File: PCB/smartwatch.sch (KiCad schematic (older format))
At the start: 66 parts, among them U1 STM32F103C8T6, U2 HM-10_MIN, U3 M25P40, U4 BMC150, U5 BMP180, U6 STC4054, U7 NCP551, U8 SH1106, X1 VIN, X10 3V3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

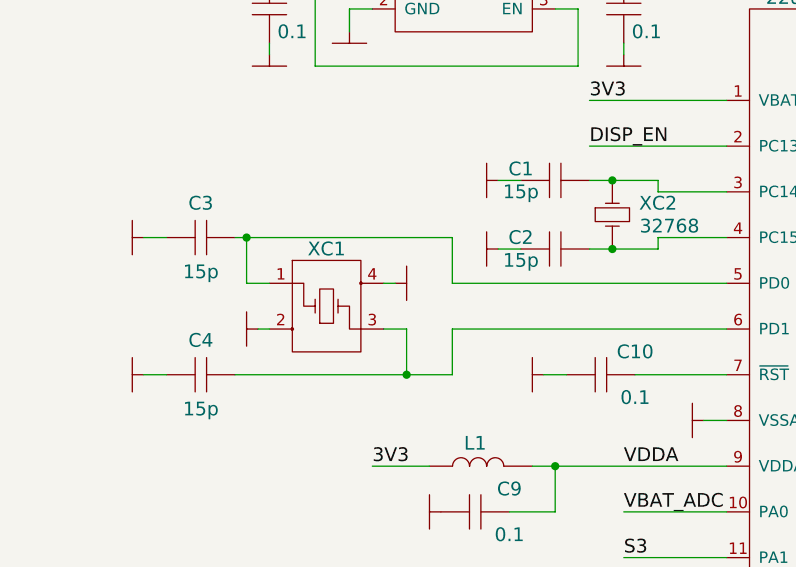
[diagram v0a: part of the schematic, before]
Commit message: Closes #2 (all values are mentioned)
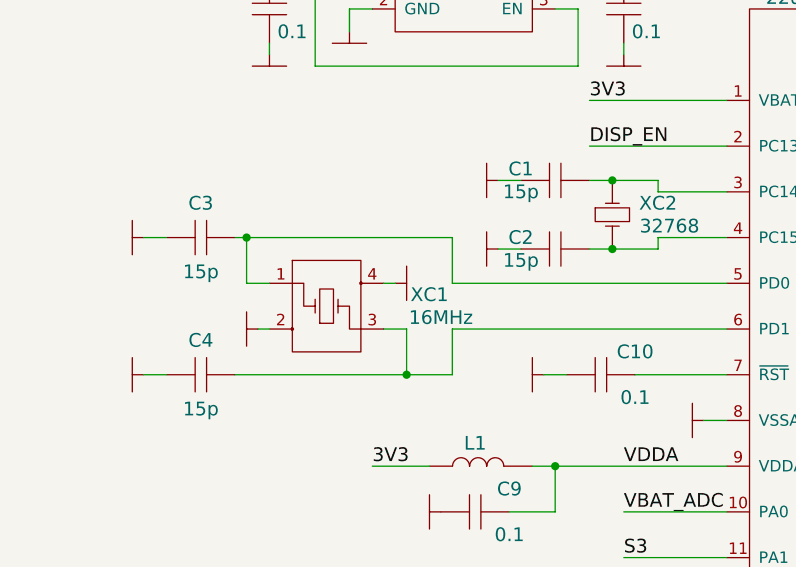
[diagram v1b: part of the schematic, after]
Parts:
- XC1: value CRYSTAL_4pin -> 16MHz
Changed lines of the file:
@@
 U 1 1 56FFF7E6
 P 1650 3100
-F 0 "XC1" H 1900 3250 60  0000 C CNN
-F 1 "CRYSTAL_4pin" H 1800 3000 60  0001 C CNN
+F 0 "XC1" H 2350 3050 60  0000 C CNN
+F 1 "16MHz" H 2400 2950 60  0000 C CNN
 F 2 "CRYSTAL:SMD_3225" H 1650 3100 60  0001 C CNN
 F 3 "" H 1650 3100 60  0000 C CNN

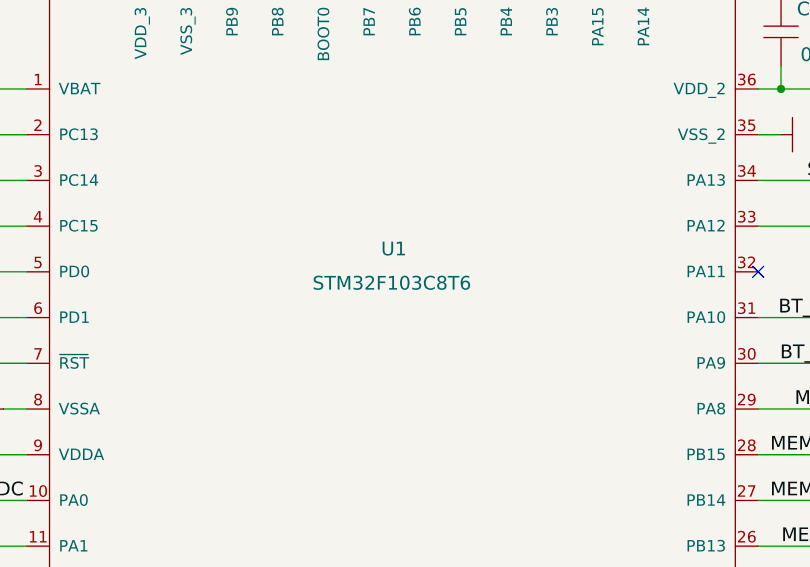
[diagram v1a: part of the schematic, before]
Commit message: Closes #10 (migration to 128kB flash)
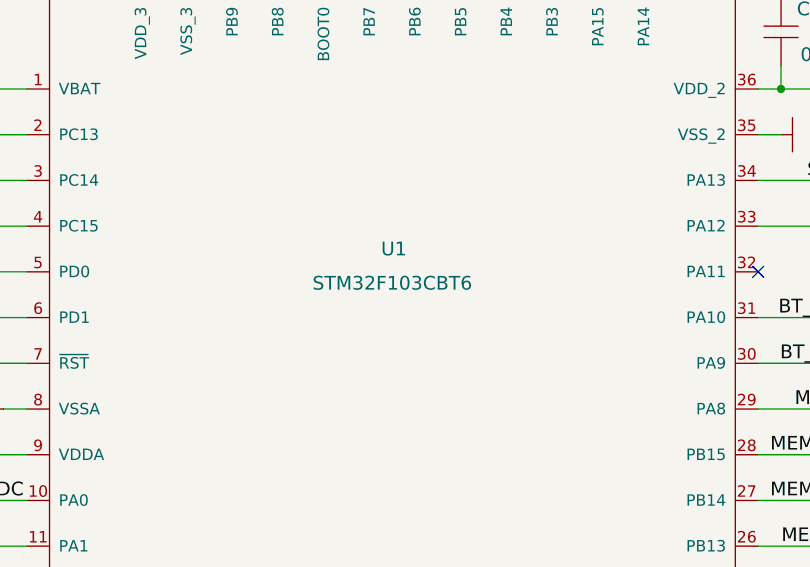
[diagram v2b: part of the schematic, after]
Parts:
- U1: value STM32F103C8T6 -> STM32F103CBT6
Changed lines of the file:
@@
 P 3650 2300
 F 0 "U1" H 5200 1600 60  0000 L CNN
-F 1 "STM32F103C8T6" H 4900 1450 60  0000 L CNN
+F 1 "STM32F103CBT6" H 4900 1450 60  0000 L CNN
 F 2 "LQFP:LQFP48" H 3650 2300 60  0001 C CNN
 F 3 "" H 3650 2300 60  0000 C CNN

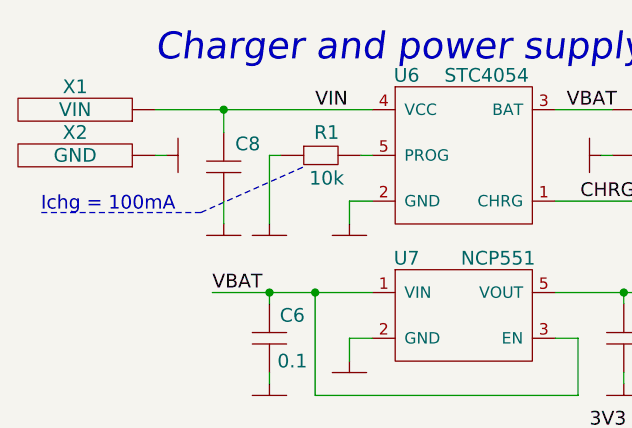
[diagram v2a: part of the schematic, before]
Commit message: Flash packer bug fix, schematic update, complete Ukrainian letters support
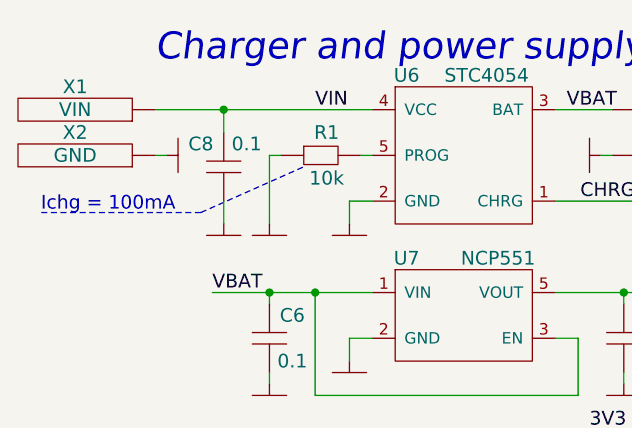
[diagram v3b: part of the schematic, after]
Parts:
- C8: value capacitor -> 0.1
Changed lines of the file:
@@
 U 1 1 5705E313
 P 1450 1300
-F 0 "C8" V 1700 1250 60  0000 R CNN
-F 1 "capacitor" H 1600 1200 60  0001 C CNN
+F 0 "C8" V 1700 1400 60  0000 C CNN
+F 1 "0.1" V 1700 1200 60  0000 C CNN
 F 2 "discrete_SMD:0402_C" H 1450 1300 60  0001 C CNN
 F 3 "" H 1450 1300 60  0000 C CNN
